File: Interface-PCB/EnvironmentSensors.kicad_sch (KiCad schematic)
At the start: 34 parts, among them IC1 SN74LVC245AN, J10 LEVEL_SENSOR, J11 LEVEL_SENSOR, J12 TEMPERATURE_SENSOR, J13 TEMPERATURE_SENSOR, J6 LEVEL_SENSOR, J7 LEVEL_SENSOR, J8 LEVEL_SENSOR, J9 LEVEL_SENSOR

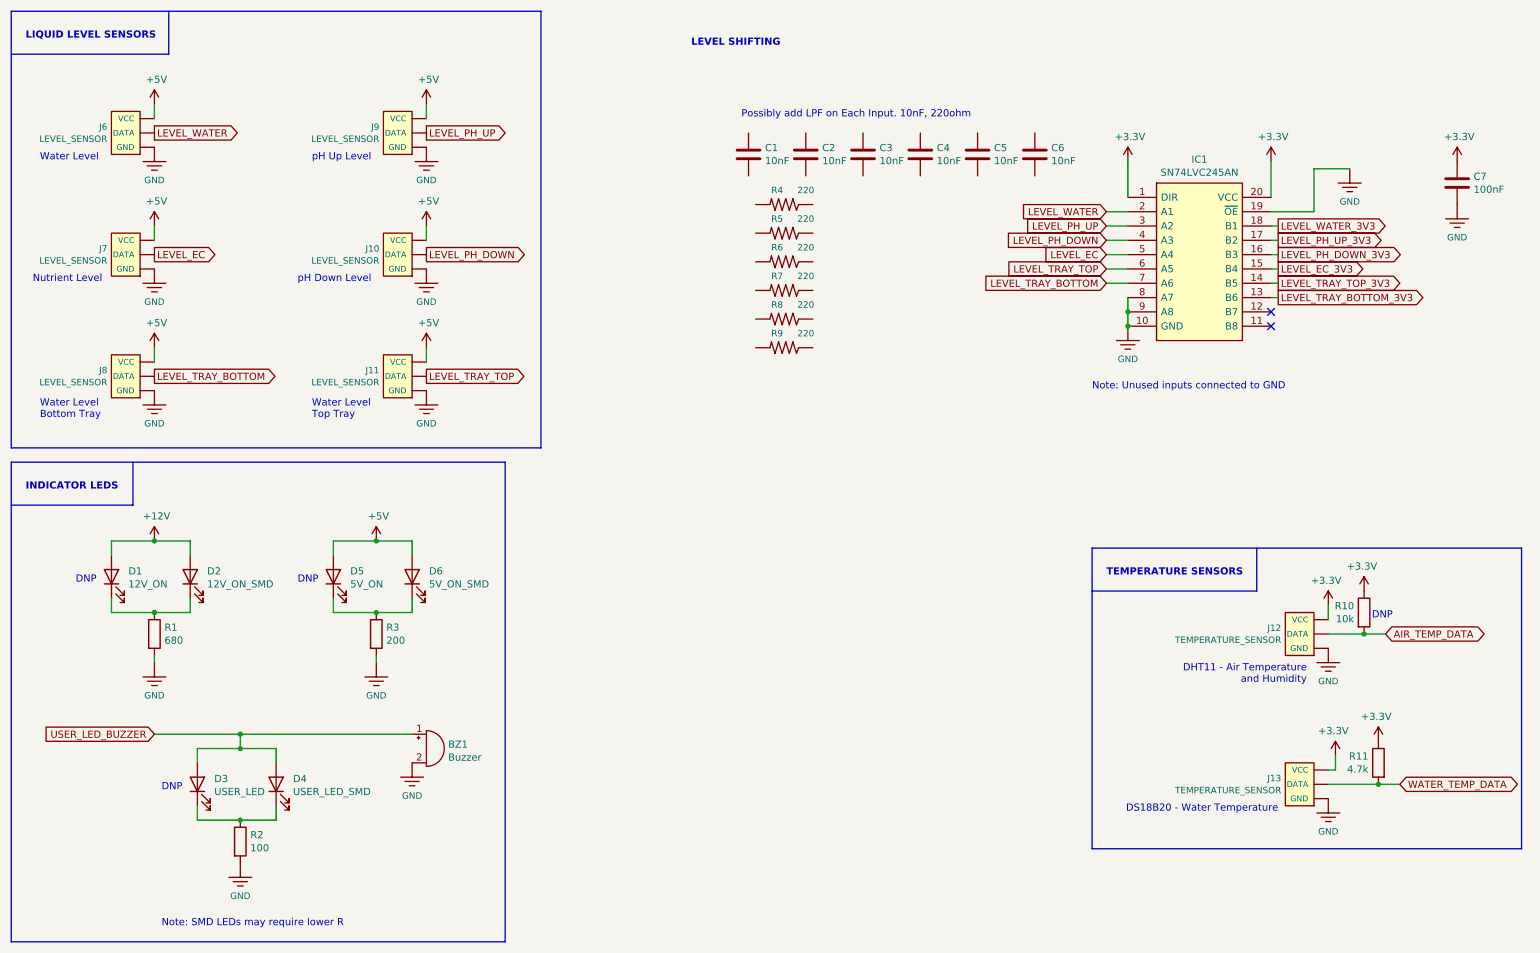
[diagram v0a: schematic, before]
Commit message: Update schematic based on breadboard tests
- Add current limiting resistors to Level Shifter output
- Add pull down resistors on all Mux outputs
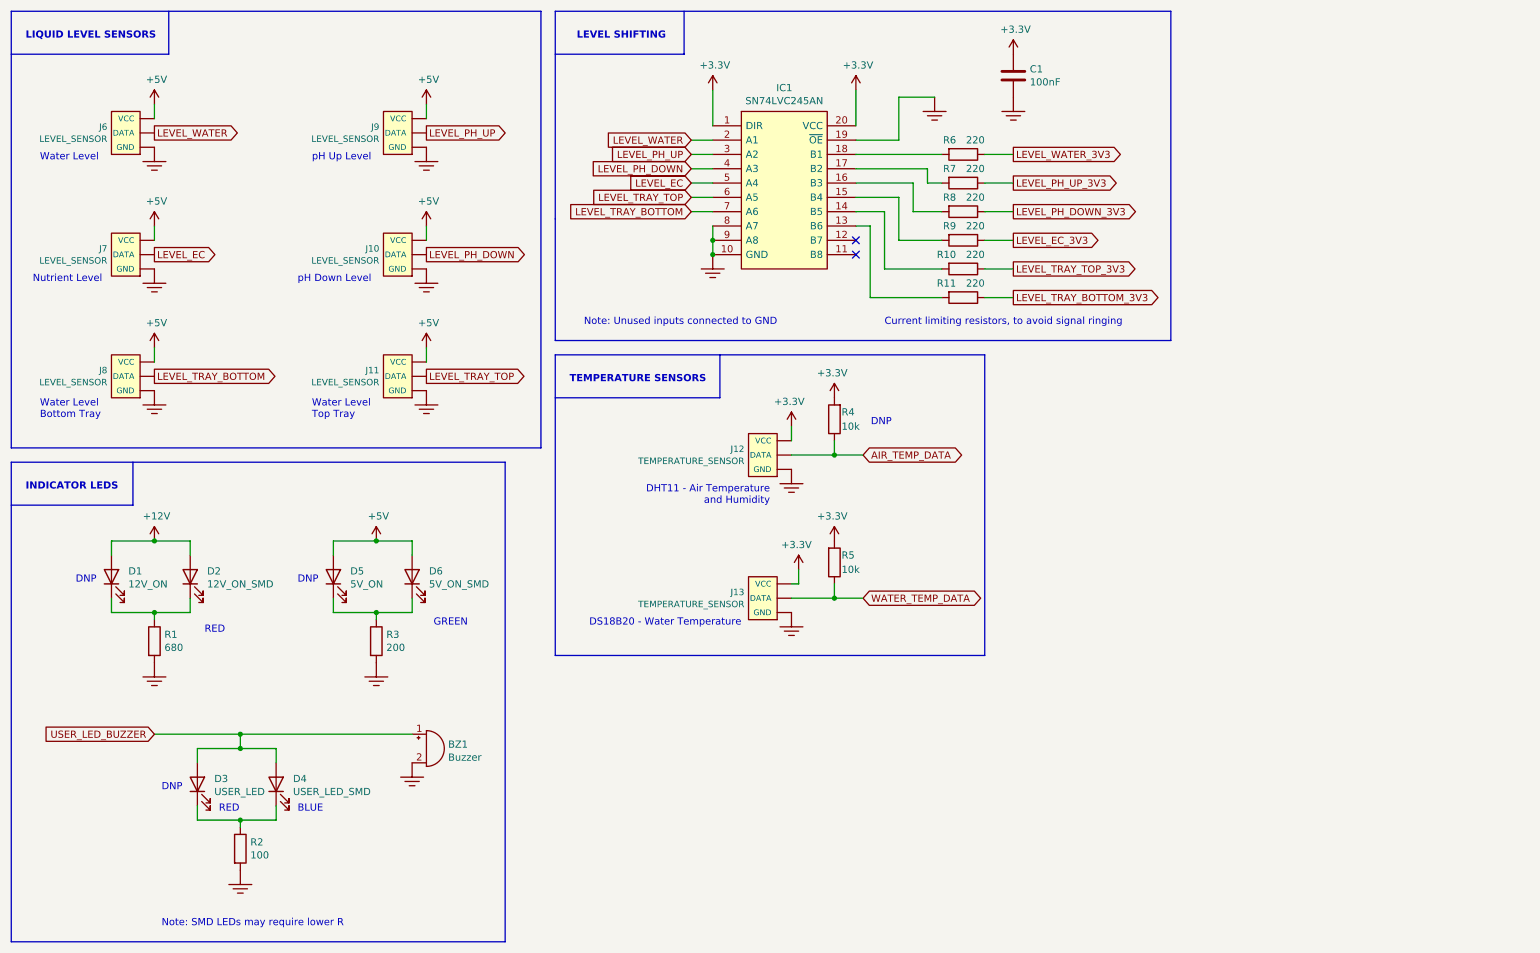
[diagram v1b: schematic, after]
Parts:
- removed C1, C2, C3, C4, C5, C6: 10nF, Capacitor_THT:C_Disc_D3.4mm_W2.1mm_P2.50mm, symbol Device:C
- removed R4, R5, R6, R7, R8, R9: 220, Resistor_THT:R_Axial_DIN0207_L6.3mm_D2.5mm_P10.16mm_Horizontal, symbol AA_Custom_Components:R
- added R10, R11, R6, R7, R8, R9: 220, Resistor_THT:R_Axial_DIN0207_L6.3mm_D2.5mm_P10.16mm_Horizontal, symbol Device:R
- R1, R2, R3: footprint Resistors:AXIAL-0.3-KIT -> Resistor_THT:R_Axial_DIN0207_L6.3mm_D2.5mm_P10.16mm_Horizontal
- R4: renamed from R10; footprint Resistors:AXIAL-0.3-KIT -> Resistor_THT:R_Axial_DIN0207_L6.3mm_D2.5mm_P10.16mm_Horizontal
- R5: renamed from R11; value 4.7k -> 10k; footprint Resistors:AXIAL-0.3-KIT -> Resistor_THT:R_Axial_DIN0207_L6.3mm_D2.5mm_P10.16mm_Horizontal
- renumbered C7 to C1
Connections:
- net +3V3: now also R4.2, R5.2; no longer R4.1, R5.1
- net AIR_TEMP_DATA: now also R4.1; no longer R4.2
- net LEVEL_EC_3V3: now also R9.1; no longer IC1.15 (B4)
- net LEVEL_PH_DOWN_3V3: now also R8.1; no longer IC1.16 (B3)
- net LEVEL_PH_UP_3V3: now also R7.1; no longer IC1.17 (B2)
- net LEVEL_TRAY_BOTTOM_3V3: now also R11.1; no longer IC1.13 (B6)
- net LEVEL_TRAY_TOP_3V3: now also R10.1; no longer IC1.14 (B5)
- net LEVEL_WATER_3V3: now also R6.1; no longer IC1.18 (B1)
- net WATER_TEMP_DATA: now also R5.1; no longer R5.2
- new net: IC1.13 (B6), R11.2
- new net: IC1.14 (B5), R10.2
- new net: IC1.15 (B4), R9.2
- new net: IC1.16 (B3), R8.2
- new net: IC1.17 (B2), R7.2
- new net: IC1.18 (B1), R6.2
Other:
- note added: "BLUE"
- note added: "Current limiting resistors, to avoid signal ringing"
- note added: "GREEN"
- note added: "RED"
- note removed: "Possibly add LPF on Each Input. 10nF, 220ohm"
- moved on the sheet: C1, IC1, J12, J13, R1, R2, R3, R4, R5

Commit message: Add test points and pads
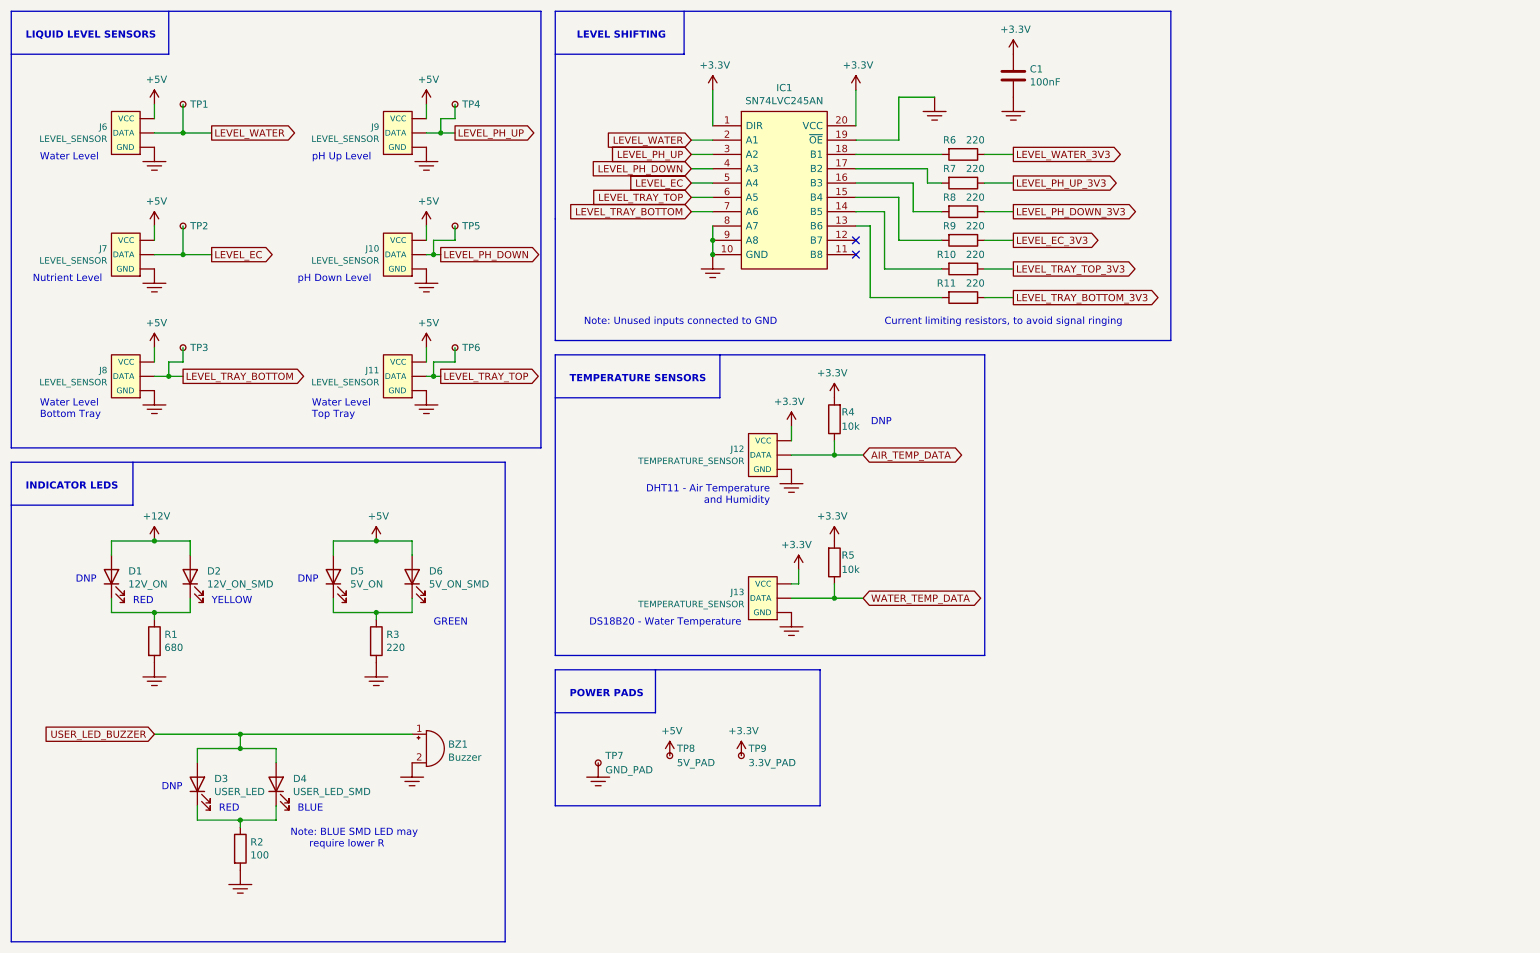
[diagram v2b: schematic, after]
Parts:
- added TP1, TP2, TP3, TP4, TP5, TP6: PAD, symbol Connector:TestPoint_Small
- added TP7: GND_PAD, symbol Connector:TestPoint_Small
- added TP8: 5V_PAD, symbol Connector:TestPoint_Small
- added TP9: 3.3V_PAD, symbol Connector:TestPoint_Small
- R3: value 200 -> 220
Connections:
- net +3V3: now also TP9.1
- net +5V: now also TP8.1
- net GND: now also TP7.1
- net LEVEL_EC: now also TP2.1
- net LEVEL_PH_DOWN: now also TP5.1
- net LEVEL_PH_UP: now also TP4.1
- net LEVEL_TRAY_BOTTOM: now also TP3.1
- net LEVEL_TRAY_TOP: now also TP6.1
- net LEVEL_WATER: now also TP1.1
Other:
- note added: "Note: BLUE SMD LED may require lower R"
- note added: "POWER PADS"
- note added: "YELLOW"
- note removed: "Note: SMD LEDs may require lower R"

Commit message: Add footprints for pads
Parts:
- R1, R10, R11, R2, R3, R4, R5, R6, R7, R8, R9: footprint Resistor_THT:R_Axial_DIN0207_L6.3mm_D2.5mm_P10.16mm_Horizontal -> AA_Custom_Components:R_SS_Axial_DIN0207_L6.3mm_D2.5mm_P10.16mm_Horizontal
- TP1, TP2, TP3, TP4, TP5, TP6: footprint (none) -> TestPoint:TestPoint_Pad_D1.5mm
- TP7, TP8, TP9: footprint (none) -> AA_Custom_Components:TestPoint_Pad_5.0x5.0mm
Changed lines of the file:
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@@
       (effects (font (size 1.27 1.27)) (justify left))
     )
-    (property "Footprint" "Resistor_THT:R_Axial_DIN0207_L6.3mm_D2.5mm_P10.16mm_Horizontal" (id 2) (at 159.512 113.03 90)
+    (property "Footprint" "AA_Custom_Components:R_SS_Axial_DIN0207_L6.3mm_D2.5mm_P10.16mm_Horizontal" (id 2) (at 159.512 113.03 90)
       (effects (font (size 1.27 1.27)) hide)
     )
@@
       (effects (font (size 1.27 1.27)) (justify right))
     )
-    (property "Footprint" "Resistor_THT:R_Axial_DIN0207_L6.3mm_D2.5mm_P10.16mm_Horizontal" (id 2) (at 163.068 87.63 90)
+    (property "Footprint" "AA_Custom_Components:R_SS_Axial_DIN0207_L6.3mm_D2.5mm_P10.16mm_Horizontal" (id 2) (at 163.068 87.63 90)
       (effects (font (size 1.27 1.27)) hide)
     )
@@
       (effects (font (size 1.27 1.27)) (justify left))
     )
-    (property "Footprint" "Resistor_THT:R_Axial_DIN0207_L6.3mm_D2.5mm_P10.16mm_Horizontal" (id 2) (at 38.862 127 90)
+    (property "Footprint" "AA_Custom_Components:R_SS_Axial_DIN0207_L6.3mm_D2.5mm_P10.16mm_Horizontal" (id 2) (at 38.862 127 90)
       (effects (font (size 1.27 1.27)) hide)
     )
@@
       (effects (font (size 1.27 1.27)) (justify left))
     )
-    (property "Footprint" "Resistor_THT:R_Axial_DIN0207_L6.3mm_D2.5mm_P10.16mm_Horizontal" (id 2) (at 78.232 127 90)
+    (property "Footprint" "AA_Custom_Components:R_SS_Axial_DIN0207_L6.3mm_D2.5mm_P10.16mm_Horizontal" (id 2) (at 78.232 127 90)
       (effects (font (size 1.27 1.27)) hide)
     )
@@
       (effects (font (size 1.27 1.27)) (justify left))
     )
-    (property "Footprint" "Resistor_THT:R_Axial_DIN0207_L6.3mm_D2.5mm_P10.16mm_Horizontal" (id 2) (at 54.102 163.83 90)
+    (property "Footprint" "AA_Custom_Components:R_SS_Axial_DIN0207_L6.3mm_D2.5mm_P10.16mm_Horizontal" (id 2) (at 54.102 163.83 90)
       (effects (font (size 1.27 1.27)) hide)
     )
@@
       (effects (font (size 1.27 1.27)) (justify right))
     )
-    (property "Footprint" "Resistor_THT:R_Axial_DIN0207_L6.3mm_D2.5mm_P10.16mm_Horizontal" (id 2) (at 184.15 54.102 90)
+    (property "Footprint" "AA_Custom_Components:R_SS_Axial_DIN0207_L6.3mm_D2.5mm_P10.16mm_Horizontal" (id 2) (at 184.15 54.102 90)
       (effects (font (size 1.27 1.27)) hide)
     )
@@
       (effects (font (size 1.27 1.27)) (justify right))
     )
-    (property "Footprint" "Resistor_THT:R_Axial_DIN0207_L6.3mm_D2.5mm_P10.16mm_Horizontal" (id 2) (at 184.15 43.942 90)
+    (property "Footprint" "AA_Custom_Components:R_SS_Axial_DIN0207_L6.3mm_D2.5mm_P10.16mm_Horizontal" (id 2) (at 184.15 43.942 90)
       (effects (font (size 1.27 1.27)) hide)
     )
@@
       (effects (font (size 1.27 1.27)) (justify left) hide)
     )
-    (property "Footprint" "" (id 2) (at 50.8 74.93 0)
+    (property "Footprint" "TestPoint:TestPoint_Pad_D1.5mm" (id 2) (at 50.8 74.93 0)
       (effects (font (size 1.27 1.27)) hide)
     )
@@
       (effects (font (size 1.27 1.27)) (justify right))
     )
-    (property "Footprint" "Resistor_THT:R_Axial_DIN0207_L6.3mm_D2.5mm_P10.16mm_Horizontal" (id 2) (at 184.15 64.262 90)
+    (property "Footprint" "AA_Custom_Components:R_SS_Axial_DIN0207_L6.3mm_D2.5mm_P10.16mm_Horizontal" (id 2) (at 184.15 64.262 90)
       (effects (font (size 1.27 1.27)) hide)
     )
@@
       (effects (font (size 1.27 1.27)) (justify right))
     )
-    (property "Footprint" "Resistor_THT:R_Axial_DIN0207_L6.3mm_D2.5mm_P10.16mm_Horizontal" (id 2) (at 184.15 59.182 90)
+    (property "Footprint" "AA_Custom_Components:R_SS_Axial_DIN0207_L6.3mm_D2.5mm_P10.16mm_Horizontal" (id 2) (at 184.15 59.182 90)
       (effects (font (size 1.27 1.27)) hide)
     )
@@
       (effects (font (size 1.27 1.27)) (justify left) hide)
     )
-    (property "Footprint" "" (id 2) (at 99.06 74.93 0)
+    (property "Footprint" "TestPoint:TestPoint_Pad_D1.5mm" (id 2) (at 99.06 74.93 0)
       (effects (font (size 1.27 1.27)) hide)
     )
@@
       (effects (font (size 1.27 1.27)) (justify left) hide)
     )
-    (property "Footprint" "" (id 2) (at 50.8 31.75 0)
+    (property "Footprint" "TestPoint:TestPoint_Pad_D1.5mm" (id 2) (at 50.8 31.75 0)
       (effects (font (size 1.27 1.27)) hide)
     )
@@
       (effects (font (size 1.27 1.27)) (justify right))
     )
-    (property "Footprint" "Resistor_THT:R_Axial_DIN0207_L6.3mm_D2.5mm_P10.16mm_Horizontal" (id 2) (at 184.15 49.022 90)
+    (property "Footprint" "AA_Custom_Components:R_SS_Axial_DIN0207_L6.3mm_D2.5mm_P10.16mm_Horizontal" (id 2) (at 184.15 49.022 90)
       (effects (font (size 1.27 1.27)) hide)
     )
@@
       (effects (font (size 1.27 1.27)) (justify left))
     )
-    (property "Footprint" "" (id 2) (at 137.16 147.32 0)
+    (property "Footprint" "AA_Custom_Components:TestPoint_Pad_5.0x5.0mm" (id 2) (at 137.16 147.32 0)
       (effects (font (size 1.27 1.27)) hide)
     )
@@
       (effects (font (size 1.27 1.27)) (justify left) hide)
     )
-    (property "Footprint" "" (id 2) (at 99.06 31.75 0)
+    (property "Footprint" "TestPoint:TestPoint_Pad_D1.5mm" (id 2) (at 99.06 31.75 0)
       (effects (font (size 1.27 1.27)) hide)
     )
@@
       (effects (font (size 1.27 1.27)) (justify left) hide)
     )
-    (property "Footprint" "" (id 2) (at 50.8 53.34 0)
+    (property "Footprint" "TestPoint:TestPoint_Pad_D1.5mm" (id 2) (at 50.8 53.34 0)
       (effects (font (size 1.27 1.27)) hide)
     )
@@
       (effects (font (size 1.27 1.27)) (justify left))
     )
-    (property "Footprint" "" (id 2) (at 124.46 148.59 0)
+    (property "Footprint" "AA_Custom_Components:TestPoint_Pad_5.0x5.0mm" (id 2) (at 124.46 148.59 0)
       (effects (font (size 1.27 1.27)) hide)
     )
@@
       (effects (font (size 1.27 1.27)) (justify left) hide)
     )
-    (property "Footprint" "" (id 2) (at 99.06 53.34 0)
+    (property "Footprint" "TestPoint:TestPoint_Pad_D1.5mm" (id 2) (at 99.06 53.34 0)
       (effects (font (size 1.27 1.27)) hide)
     )
@@
       (effects (font (size 1.27 1.27)) (justify left))
     )
-    (property "Footprint" "" (id 2) (at 149.86 147.32 0)
+    (property "Footprint" "AA_Custom_Components:TestPoint_Pad_5.0x5.0mm" (id 2) (at 149.86 147.32 0)
       (effects (font (size 1.27 1.27)) hide)
     )
@@
       (effects (font (size 1.27 1.27)) (justify right))
     )
-    (property "Footprint" "Resistor_THT:R_Axial_DIN0207_L6.3mm_D2.5mm_P10.16mm_Horizontal" (id 2) (at 184.15 38.862 90)
-      (effects (font (size 1.27 1.27)) hide)
-    )
+    (property "Footprint" "AA_Custom_Components:R_SS_Axial_DIN0207_L6.3mm_D2.5mm_P10.16mm_Horizontal" (id 2) (at 184.15 38.862 90)
+      (effects (font (size 1.27 1.27)) hide)
+    )

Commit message: Add breakout board and IC footprints
- MUX
- Motor Driver
- PDIP ICs
- LEDs
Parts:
- D2, D4, D6: footprint LED_SMD:LED_1206_3216Metric_Pad1.42x1.75mm_HandSolder -> AA_Custom_Components:LED_SS_1206_3216Metric_Pad1.42x1.75mm_HandSolder
- IC1: footprint Package_DIP:DIP-20_W7.62mm_LongPads -> AA_Custom_Components:DIP-20_W7.62mm_Socket_IC; Digikey_Part_Number (none) -> 296-8503-5-ND; Height 5.08 -> (none); Manufacturer_Part_Number 296-8503-5-ND -> (none)
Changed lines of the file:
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@@
       (effects (font (size 1.27 1.27)) (justify right))
     )
-    (property "Footprint" "LED_SMD:LED_1206_3216Metric_Pad1.42x1.75mm_HandSolder" (id 2) (at 46.99 115.57 0)
+    (property "Footprint" "AA_Custom_Components:LED_SS_1206_3216Metric_Pad1.42x1.75mm_HandSolder" (id 2) (at 46.99 115.57 0)
       (effects (font (size 1.27 1.27)) hide)
     )
@@
       (effects (font (size 1.27 1.27)) (justify right))
     )
-    (property "Footprint" "LED_SMD:LED_1206_3216Metric_Pad1.42x1.75mm_HandSolder" (id 2) (at 86.36 115.57 0)
+    (property "Footprint" "AA_Custom_Components:LED_SS_1206_3216Metric_Pad1.42x1.75mm_HandSolder" (id 2) (at 86.36 115.57 0)
       (effects (font (size 1.27 1.27)) hide)
     )
@@
     (property "Reference" "IC1" (id 0) (at 152.4 28.829 0))
     (property "Value" "SN74LVC245AN" (id 1) (at 152.4 31.1404 0))
-    (property "Footprint" "Package_DIP:DIP-20_W7.62mm_LongPads" (id 2) (at 161.29 33.02 0)
-      (effects (font (size 1.27 1.27)) (justify left) hide)
-    )
-    (property "Datasheet" "http://www.ti.com/lit/gpn/sn74hct245" (id 3) (at 161.29 35.56 0)
-      (effects (font (size 1.27 1.27)) (justify left) hide)
-    )
-    (property "Description" "Octal Bus Transceivers With 3-State Outputs" (id 4) (at 161.29 38.1 0)
-      (effects (font (size 1.27 1.27)) (justify left) hide)
-    )
-    (property "Height" "5.08" (id 5) (at 161.29 40.64 0)
+    (property "Footprint" "AA_Custom_Components:DIP-20_W7.62mm_Socket_IC" (id 2) (at 161.29 33.02 0)
+      (effects (font (size 1.27 1.27)) (justify left) hide)
+    )
+    (property "Datasheet" "https://www.ti.com/lit/ds/scas218x/scas218x.pdf" (id 3) (at 161.29 35.56 0)
       (effects (font (size 1.27 1.27)) (justify left) hide)
     )
@@
       (effects (font (size 1.27 1.27)) (justify left) hide)
     )
-    (property "Manufacturer_Part_Number" "296-8503-5-ND" (id 7) (at 161.29 45.72 0)
+    (property "Digikey_Part_Number" "296-8503-5-ND" (id 8) (at 161.29 45.72 0)
       (effects (font (size 1.27 1.27)) (justify left) hide)
     )
@@
       (effects (font (size 1.27 1.27)) (justify right))
     )
-    (property "Footprint" "LED_SMD:LED_1206_3216Metric_Pad1.42x1.75mm_HandSolder" (id 2) (at 62.23 152.4 0)
-      (effects (font (size 1.27 1.27)) hide)
-    )
+    (property "Footprint" "AA_Custom_Components:LED_SS_1206_3216Metric_Pad1.42x1.75mm_HandSolder" (id 2) (at 62.23 152.4 0)
+      (effects (font (size 1.27 1.27)) hide)
+    )
